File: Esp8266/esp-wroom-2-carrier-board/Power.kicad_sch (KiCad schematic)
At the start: 9 parts, among them U3 TPS5410DR

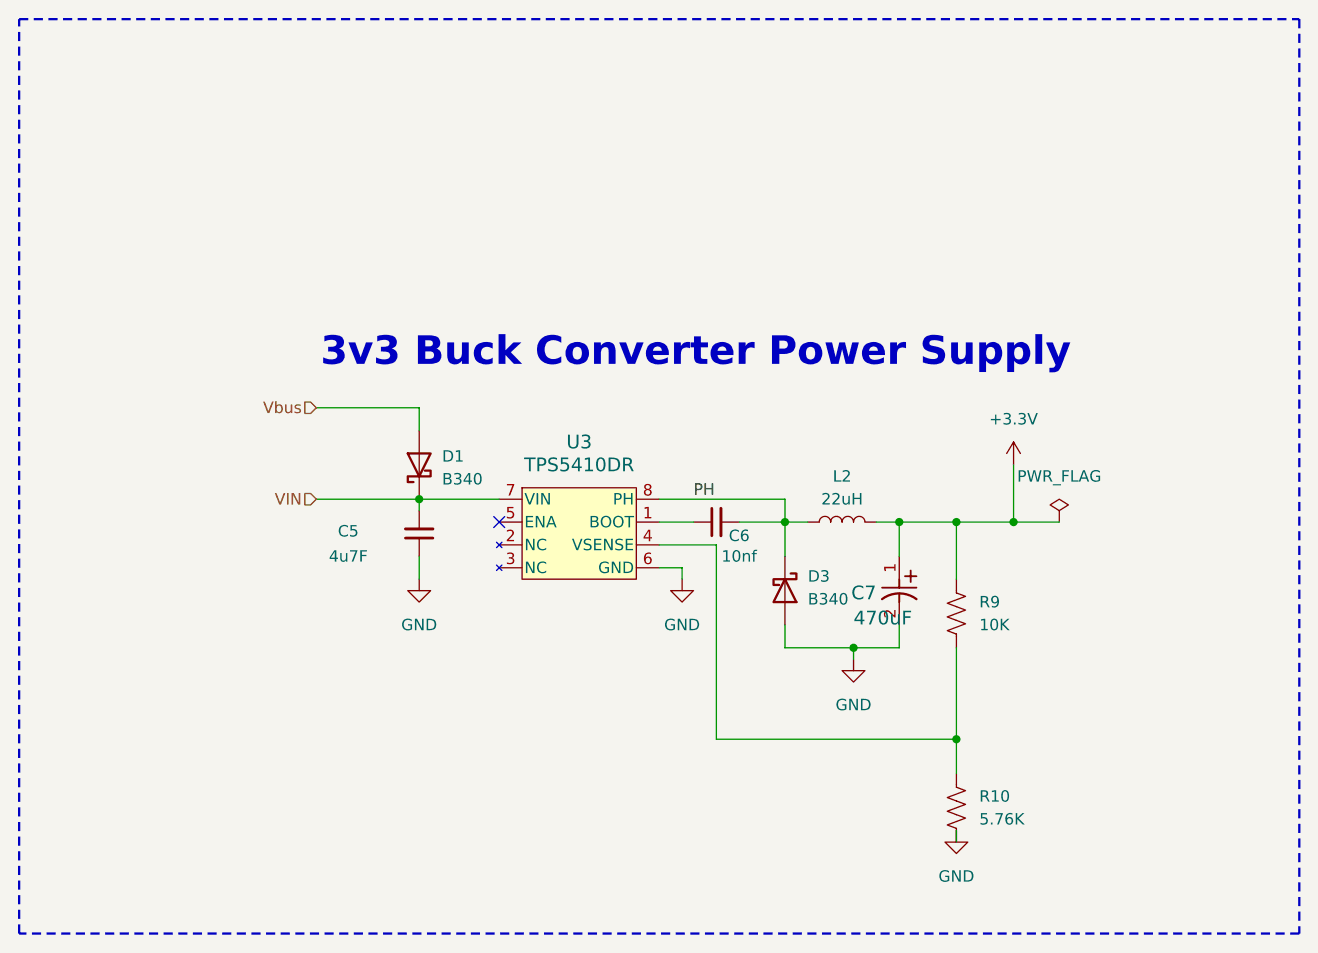
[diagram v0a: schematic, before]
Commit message: capacitor layout
Changed capacitor position to front layer to have enough clearance on bottom layer
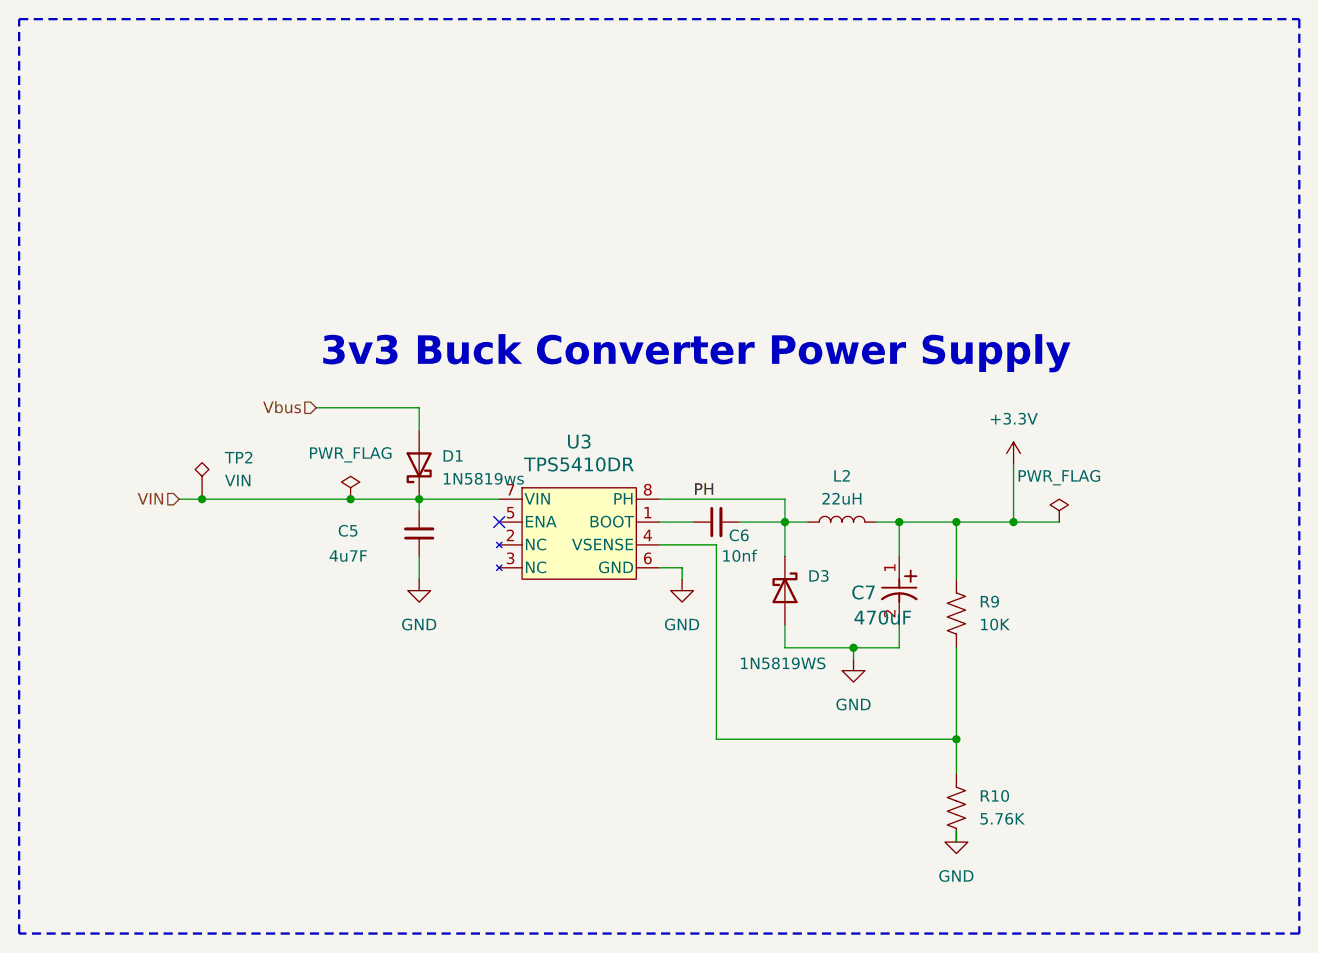
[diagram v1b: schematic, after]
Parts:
- added TP2: VIN, TestPoint:TestPoint_THTPad_D1.0mm_Drill0.5mm, symbol Connector:TestPoint_Alt
- D1: value B340 -> 1N5819ws; footprint Diode_SMD:D_SMC -> Diode_SMD:D_SOD-323; symbol Diode:B340 -> Diode:1N5819WS
- D3: value B340 -> 1N5819WS; footprint Diode_SMD:D_SMC -> Diode_SMD:D_SOD-323; symbol Diode:B340 -> Diode:1N5819WS
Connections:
- net VIN: now also TP2.1
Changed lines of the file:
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@@
+	)
+	(junction
+		(at 91.44 78.74)
+		(diameter 0)
+		(color 0 0 0 0)
 	)
 	(junction
@@
 	)
 	(junction
+		(at 107.95 78.74)
+		(diameter 0)
+		(color 0 0 0 0)
+	)
+	(junction
 		(at 168.91 81.28)
 		(diameter 0)
@@
 	(wire
 		(pts
-			(xy 104.14 78.74) (xy 115.57 78.74)
+			(xy 88.9 78.74) (xy 91.44 78.74)
 		)
 		(stroke
@@
 	(wire
 		(pts
+			(xy 91.44 78.74) (xy 107.95 78.74)
+		)
+		(stroke
+			(width 0)
+			(type default)
+		)
+	)
+	(wire
+		(pts
 			(xy 181.61 81.28) (xy 175.26 81.28)
 		)
@@
 		(pts
 			(xy 148.59 83.82) (xy 142.24 83.82)
+		)
+		(stroke
+			(width 0)
+			(type default)
+		)
+	)
+	(wire
+		(pts
+			(xy 107.95 78.74) (xy 115.57 78.74)
 		)
 		(stroke
@@
 	(hierarchical_label "VIN"
 		(shape input)
-		(at 104.14 78.74 180)
+		(at 88.9 78.74 180)
 		(effects
 			(font
@@
 	)
 	(symbol
-		(lib_id "Diode:B340")
+		(lib_id "Diode:1N5819WS")
 		(at 115.57 74.93 90)
 		(unit 1)
@@
 			)
 		)
-		(property "Value" "B340"
+		(property "Value" "1N5819ws"
 			(at 118.11 76.5175 90)
 			(effects
@@
 			)
 		)
-		(property "Footprint" "Diode_SMD:D_SMC"
+		(property "Footprint" "Diode_SMD:D_SOD-323"
 			(at 120.015 74.93 0)
 			(effects
@@
 			)
 		)
-		(property "Datasheet" "http://www.jameco.com/Jameco/Products/ProdDS/1538777.pdf"
+		(property "Datasheet" "https://datasheet.lcsc.com/lcsc/2204281430_Guangdong-Hottech-1N5819WS_C191023.pdf"
 			(at 115.57 74.93 0)
 			(effects
@@
 			)
 		)
-		(property "Description" "40V 3A Schottky Barrier Rectifier Diode, SMC"
+		(property "Description" "40V 600mV@1A 1A SOD-323 Schottky Barrier Diodes, SOD-323"
 			(at 115.57 74.93 0)
 			(effects
@@
 				(path "/02e826db-efcd-428f-8d48-cef0de8c3fb5/ce7027db-382f-4a3d-842f-452933e73176"
 					(reference "C6")
+					(unit 1)
+				)
+			)
+		)
+	)
+	(symbol
+		(lib_id "power:PWR_FLAG")
+		(at 107.95 78.74 0)
+		(unit 1)
+		(exclude_from_sim no)
+		(in_bom yes)
+		(on_board yes)
+		(dnp no)
+		(fields_autoplaced yes)
+		(property "Reference" "#FLG01"
+			(at 107.95 76.835 0)
+			(effects
+				(font
+					(size 1.27 1.27)
+				)
+				(hide yes)
+			)
+		)
+		(property "Value" "PWR_FLAG"
+			(at 107.95 73.66 0)
+			(effects
+				(font
+					(size 1.27 1.27)
+				)
+			)
+		)
+		(property "Footprint" ""
+			(at 107.95 78.74 0)
+			(effects
+				(font
+					(size 1.27 1.27)
+				)
+				(hide yes)
+			)
+		)
+		(property "Datasheet" "~"
+			(at 107.95 78.74 0)
+			(effects
+				(font
+					(size 1.27 1.27)
+				)
+				(hide yes)
+			)
+		)
+		(property "Description" "Special symbol for telling ERC where power comes from"
+			(at 107.95 78.74 0)
+			(effects
+				(font
+					(size 1.27 1.27)
+				)
+				(hide yes)
+			)
+		)
+		(pin "1"
+		)
+		(instances
+			(project ""
+				(path "/02e826db-efcd-428f-8d48-cef0de8c3fb5/ce7027db-382f-4a3d-842f-452933e73176"
+					(reference "#FLG01")
 					(unit 1)
 				)
@@
 	)
 	(symbol
-		(lib_id "Diode:B340")
+		(lib_id "Diode:1N5819WS")
 		(at 156.21 88.9 270)
 		(unit 1)
@@
 		(on_board yes)
 		(dnp no)
-		(fields_autoplaced yes)
 		(property "Reference" "D3"
-			(at 158.75 87.3124 90)
+			(at 158.75 87.3125 90)
 			(effects
 				(font
@@
 			)
 		)
-		(property "Value" "B340"
-			(at 158.75 89.8524 90)
+		(property "Value" "1N5819WS"
+			(at 151.13 97.028 90)
 			(effects
 				(font
@@
 			)
 		)
-		(property "Footprint" "Diode_SMD:D_SMC"
+		(property "Footprint" "Diode_SMD:D_SOD-323"
 			(at 151.765 88.9 0)
 			(effects
@@
 			)
 		)
-		(property "Datasheet" "http://www.jameco.com/Jameco/Products/ProdDS/1538777.pdf"
+		(property "Datasheet" "https://datasheet.lcsc.com/lcsc/2204281430_Guangdong-Hottech-1N5819WS_C191023.pdf"
 			(at 156.21 88.9 0)
 			(effects
@@
 			)
 		)
-		(property "Description" "40V 3A Schottky Barrier Rectifier Diode, SMC"
+		(property "Description" "40V 600mV@1A 1A SOD-323 Schottky Barrier Diodes, SOD-323"
 			(at 156.21 88.9 0)
 			(effects
@@
 					(unit 1)
 				)
+			)
+		)
+	)
+	(symbol
+		(lib_id "Connector:TestPoint_Alt")
+		(at 91.44 78.74 0)
+		(unit 1)
+		(exclude_from_sim no)
+		(in_bom yes)
+		(on_board yes)
+		(dnp no)
+		(fields_autoplaced yes)
+		(property "Reference" "TP2"
+			(at 93.98 74.168 0)
+			(effects
+				(font
+					(size 1.27 1.27)
+				)
+				(justify left)
+			)
+		)
+		(property "Value" "VIN"
+			(at 93.98 76.708 0)
+			(effects
+				(font
+					(size 1.27 1.27)
+				)
+				(justify left)
+			)
+		)
+		(property "Footprint" "TestPoint:TestPoint_THTPad_D1.0mm_Drill0.5mm"
+			(at 96.52 78.74 0)
+			(effects
+				(font
+					(size 1.27 1.27)
+				)
+				(hide yes)
+			)
+		)
+		(property "Datasheet" "~"
+			(at 96.52 78.74 0)
+			(effects
+				(font
+					(size 1.27 1.27)
+				)
+				(hide yes)
+			)
+		)
+		(property "Description" "test point (alternative shape)"
+			(at 91.44 78.74 0)
+			(effects
+				(font
+					(size 1.27 1.27)
+				)
+				(hide yes)
+			)
+		)
+		(pin "1"
+		)
+		(instances
+			(project ""
+				(path "/02e826db-efcd-428f-8d48-cef0de8c3fb5/ce7027db-382f-4a3d-842f-452933e73176"
+					(reference "TP2")
+					(unit 1)
+				)
